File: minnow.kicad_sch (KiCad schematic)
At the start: 66 parts, among them J3 PicoBlade, J3 USB_C_Receptacle_Dev, J3 USB_C_Receptacle_Host, J4 ARM_JTAG_SWD_10_Male, J4 VCCIO_EXT, SW1 SW_DIP_x04, U1 FT230XQ, U2 PI5A3157CEX, U3 PI5A3157CEX, U4 USB3740B-AI2, U5 SiP32432DR3

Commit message: README started
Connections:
- net SWDCLK renamed SWCLK
- net SWDO renamed SWO
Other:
- note added: "Default: SWO and NRESET for full SWD interface. Switched: UART RXD/TXD for USB UART. Can use JP1/2 to isolate from FT or switch RX/TX."
- note removed: "Default: SWDO and NRESET for full SWD interface. Switched: UART RXD/TXD for USB UART. Can use JP1/2 to isolate from FT or switch RX/TX."
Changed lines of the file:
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@@
   (title_block
     (title "Minnow - USB-C DAM Tool")
-    (rev "0")
+    (date "2023-05-19")
+    (rev "1")
     (company "JBR Engineering Research Ltd")
     (comment 1 "J.Whittington 2023")
@@
     (effects (font (size 1.27 1.27) italic) (justify left bottom))
   )
-  (text "Default: SWDO and NRESET for full SWD interface.\nSwitched: UART RXD/TXD for USB UART.\nCan use JP1/2 to isolate from FT or switch RX/TX."
+  (text "Default: SWO and NRESET for full SWD interface.\nSwitched: UART RXD/TXD for USB UART.\nCan use JP1/2 to isolate from FT or switch RX/TX."
     (at 201.168 154.432 0)
     (effects (font (size 1.27 1.27)) (justify left bottom))
@@
     (effects (font (size 1.27 1.27)) (justify right bottom))
   )
-  (label "SWDCLK" (at 350.012 71.374 180) (fields_autoplaced)
+  (label "SWCLK" (at 350.012 71.374 180) (fields_autoplaced)
     (effects (font (size 1.27 1.27)) (justify right bottom))
   )
@@
     (effects (font (size 1.27 1.27)) (justify right bottom))
   )
-  (label "SWDCLK" (at 370.078 202.438 180) (fields_autoplaced)
+  (label "SWCLK" (at 370.078 202.438 180) (fields_autoplaced)
     (effects (font (size 1.27 1.27)) (justify right bottom))
   )
@@
     (effects (font (size 1.27 1.27)) (justify left bottom))
   )
-  (label "SWDO" (at 189.738 220.472 180) (fields_autoplaced)
+  (label "SWO" (at 189.738 220.472 180) (fields_autoplaced)
     (effects (font (size 1.27 1.27)) (justify right bottom))
   )
@@
     (effects (font (size 1.27 1.27)) (justify left bottom))
   )
-  (label "SWDCLK" (at 365.252 158.75 180) (fields_autoplaced)
+  (label "SWCLK" (at 365.252 158.75 180) (fields_autoplaced)
     (effects (font (size 1.27 1.27)) (justify right bottom))
   )
@@
     (effects (font (size 1.27 1.27)) (justify left bottom))
   )
-  (label "SWDO" (at 365.252 161.29 180) (fields_autoplaced)
+  (label "SWO" (at 365.252 161.29 180) (fields_autoplaced)
     (effects (font (size 1.27 1.27)) (justify right bottom))
   )
@@
     (effects (font (size 1.27 1.27)) (justify left bottom))
   )
-  (label "SWDCLK" (at 350.012 86.614 180) (fields_autoplaced)
+  (label "SWCLK" (at 350.012 86.614 180) (fields_autoplaced)
     (effects (font (size 1.27 1.27)) (justify right bottom))
   )
@@
     (effects (font (size 1.27 1.27)) (justify left bottom))
   )
-  (label "SWDO" (at 370.078 207.518 180) (fields_autoplaced)
+  (label "SWO" (at 370.078 207.518 180) (fields_autoplaced)
     (effects (font (size 1.27 1.27)) (justify right bottom))
   )

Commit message: update README for R1 delivery
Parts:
- FB1: MPN LI0603E151R-10 -> LI0603G121R-10; SKU 240-2366-1-ND -> 240-2367-2-ND
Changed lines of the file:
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@@
       (effects (font (size 1.27 1.27)) hide)
     )
-    (property "Description" "150 Ohms @ 100 MHz 1 Power, Signal Line Ferrite Bead 0603 (1608 Metric) 500mA 250mOhm" (at 114.3 40.64 0)
+    (property "Description" "120 Ohms @ 100 MHz 1 Power, Signal Line Ferrite Bead 0603 (1608 Metric) 1A 200mOhm" (at 114.3 40.64 0)
       (effects (font (size 1.27 1.27)) hide)
     )
@@
       (effects (font (size 1.27 1.27)) hide)
     )
-    (property "MPN" "LI0603E151R-10" (at 114.3 40.64 0)
+    (property "MPN" "LI0603G121R-10" (at 114.3 40.64 0)
       (effects (font (size 1.27 1.27)) hide)
     )
-    (property "SKU" "240-2366-1-ND" (at 114.3 40.64 0)
+    (property "SKU" "240-2367-2-ND" (at 114.3 40.64 0)
       (effects (font (size 1.27 1.27)) hide)
     )
@@
       (effects (font (size 1.27 1.27)) hide)
     )
+    (property "Notes" "" (at 114.3 40.64 0)
+      (effects (font (size 1.27 1.27)) hide)
+    )
+    (property "Config" "" (at 114.3 40.64 0)
+      (effects (font (size 1.27 1.27)) hide)
+    )

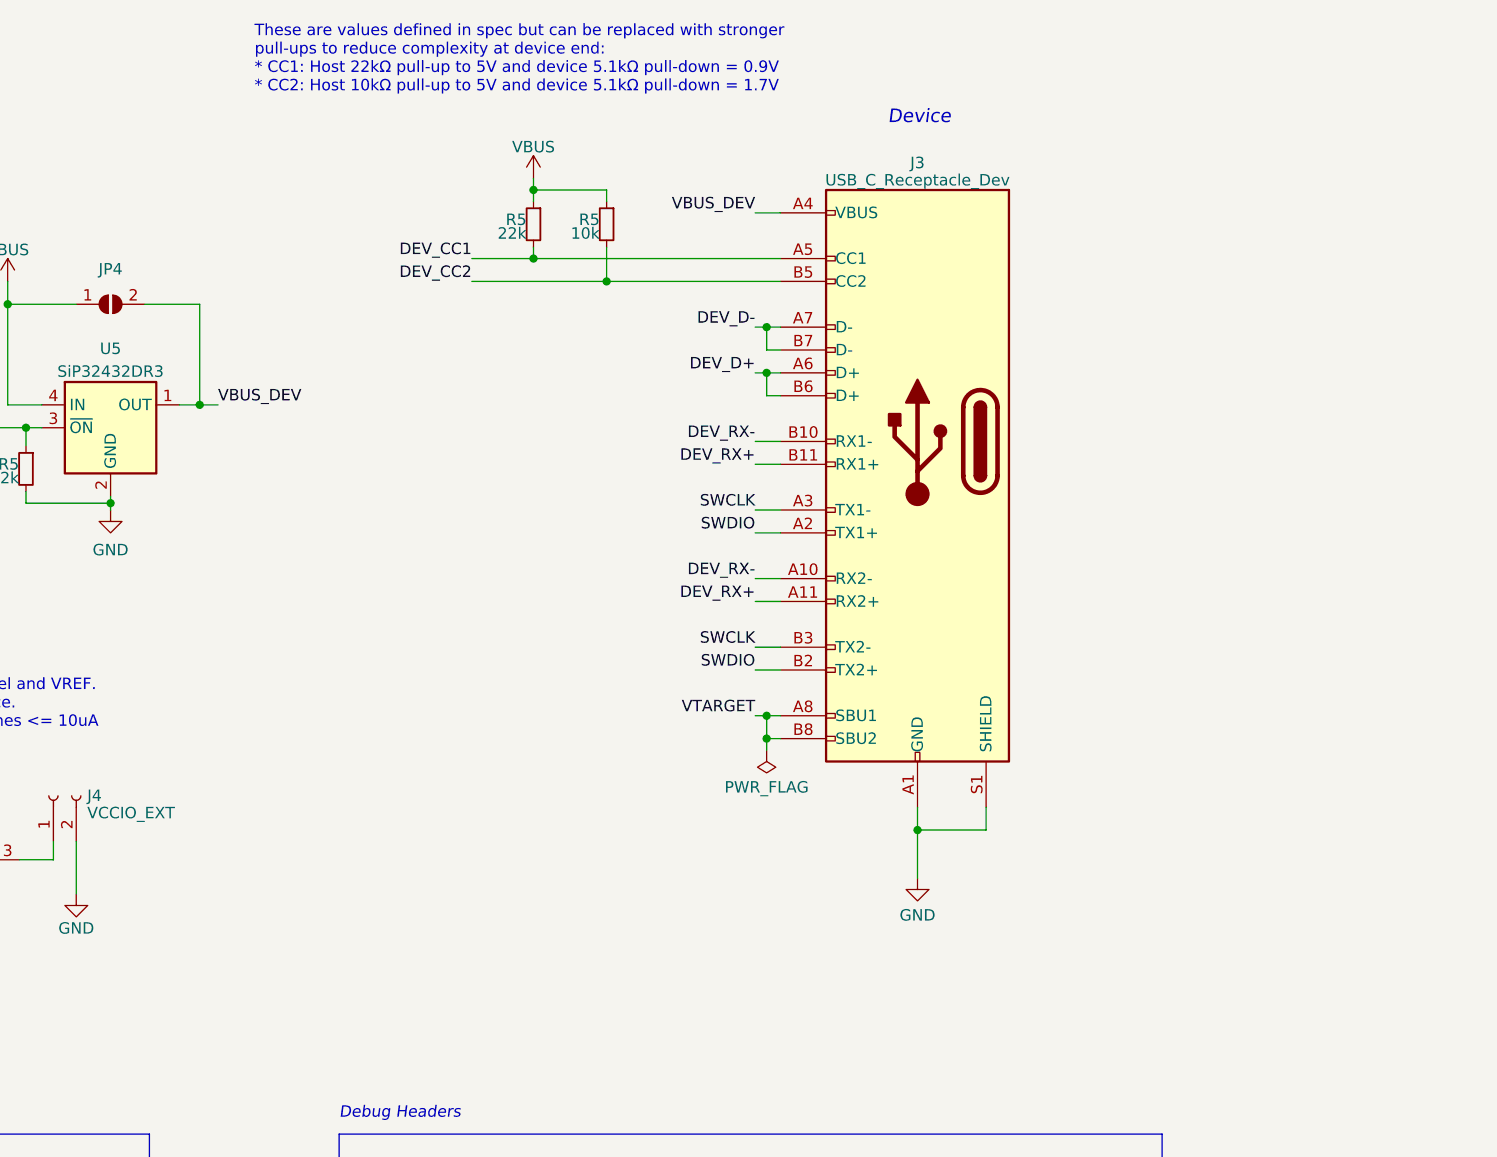
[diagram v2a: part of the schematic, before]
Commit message: plug not receptacle for device (TS)
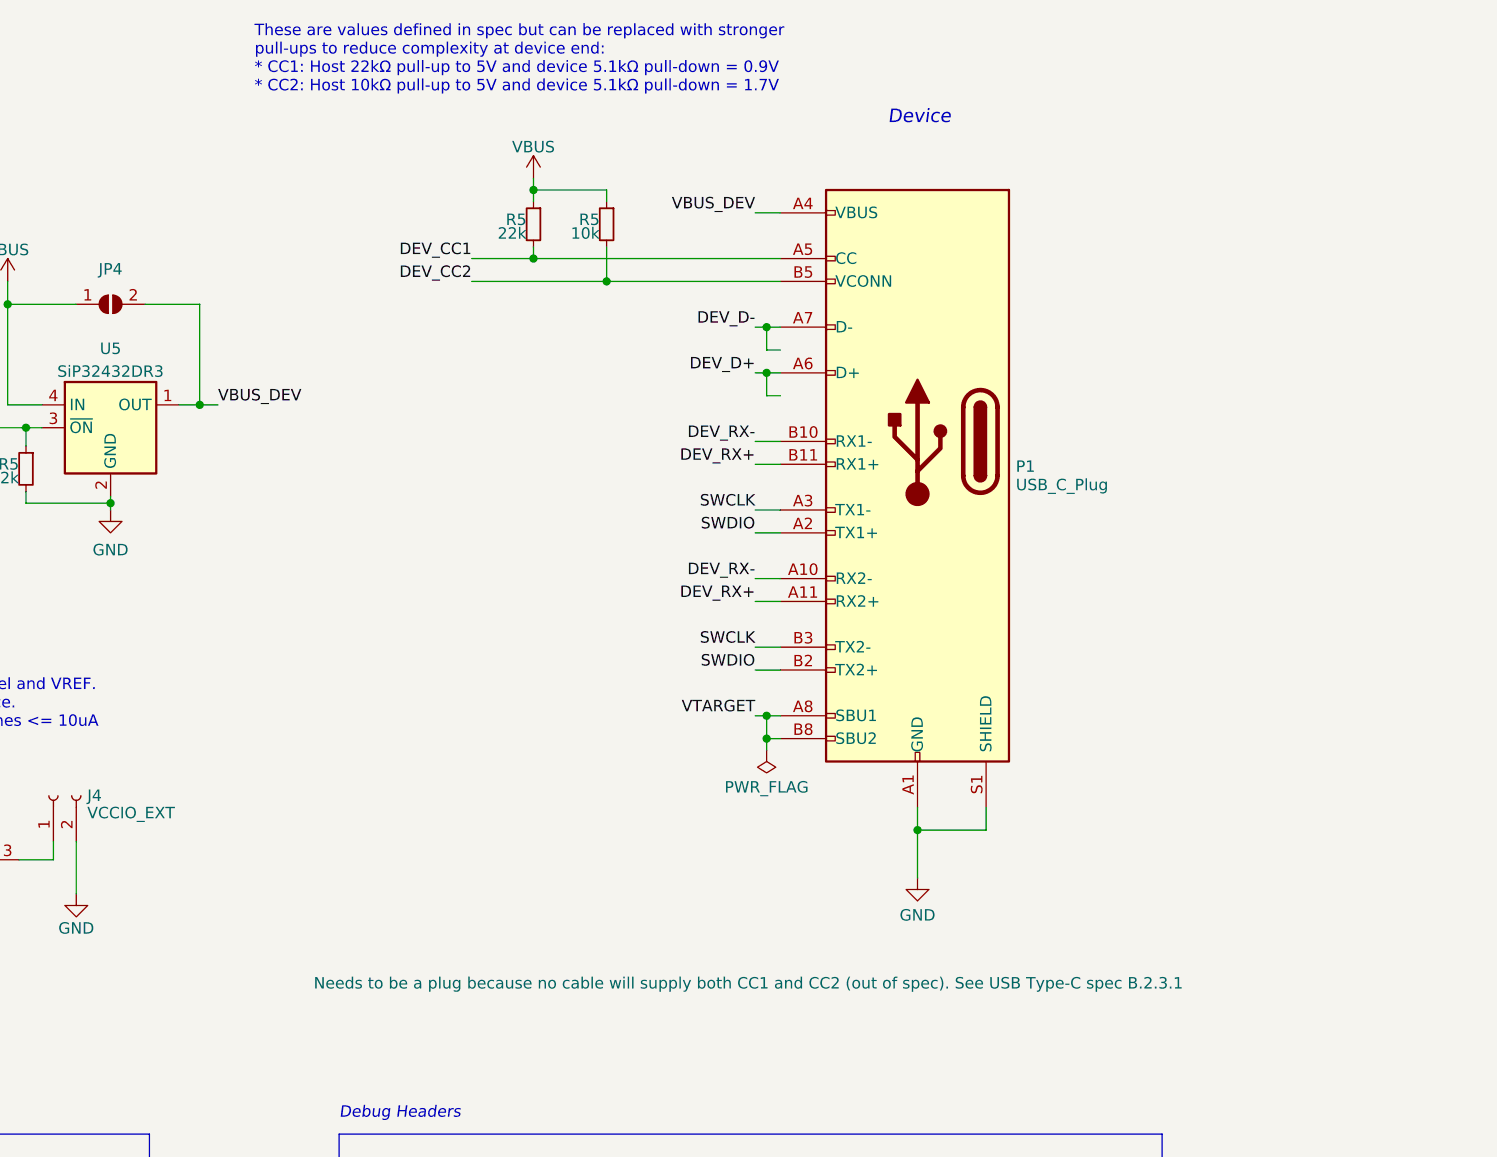
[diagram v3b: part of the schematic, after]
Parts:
- removed J3: USB_C_Receptacle_Dev, Connector_USB:USB_C_Receptacle_Amphenol_12401610E4-2A, symbol Connector:USB_C_Receptacle
- added P1: USB_C_Plug, Connector_USB:USB_C_Plug_Molex_105444, symbol Connector:USB_C_Plug
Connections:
- net DEV_CC1: now also P1.A5 (CC)
- net DEV_CC2: now also P1.B5 (VCONN)
- net DEV_D+: now also P1.A6 (D+)
- net DEV_D-: now also P1.A7 (D-)
- net DEV_RX+: now also P1.A11 (RX2+), P1.B11 (RX1+)
- net DEV_RX-: now also P1.A10 (RX2-), P1.B10 (RX1-)
- net GND: now also P1.A1 (GND), P1.A12 (GND), P1.B1 (GND), P1.B12 (GND), P1.S1 (SHIELD)
- net SWCLK: now also P1.A3 (TX1-), P1.B3 (TX2-)
- net SWDIO: now also P1.A2 (TX1+), P1.B2 (TX2+)
- net VBUS_DEV: now also P1.A4 (VBUS), P1.A9 (VBUS), P1.B4 (VBUS), P1.B9 (VBUS)
- net VTARGET: now also P1.A8 (SBU1), P1.B8 (SBU2)
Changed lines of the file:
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@@
   (title_block
     (title "Minnow - USB-C DAM Tool")
-    (date "2023-05-19")
-    (rev "1")
+    (date "2023-06-22")
+    (rev "2")
     (company "JBR Engineering Research Ltd")
     (comment 1 "J.Whittington 2023")
@@
     )
   )
-  (symbol (lib_id "Connector:USB_C_Receptacle") (at 368.046 63.754 0) (mirror y) (unit 1)
-    (in_bom yes) (on_board yes) (dnp no)
-    (property "Reference" "J3" (at 368.046 32.8041 0)
-      (effects (font (size 1.27 1.27)))
-    )
-    (property "Value" "USB_C_Receptacle_Dev" (at 368.046 34.7251 0)
-      (effects (font (size 1.27 1.27)))
-    )
-    (property "Footprint" "Connector_USB:USB_C_Receptacle_Amphenol_12401610E4-2A" (at 364.236 63.754 0)
-      (effects (font (size 1.27 1.27)) hide)
-    )
-    (property "Datasheet" "https://media.digikey.com/pdf/Data%20Sheets/Amphenol%20PDFs/12401832E402A_Dwg_RevX1_04-25-17.pdf" (at 364.236 63.754 0)
-      (effects (font (size 1.27 1.27)) hide)
-    )
-    (property "Description" "USB-C (USB TYPE-C) USB 3.2 Gen 2 (USB 3.1 Gen 2, Superspeed + (USB 3.1)) Receptacle Connector 24 Position Surface Mount, Right Angle; Through Hole" (at 368.046 63.754 0)
-      (effects (font (size 1.27 1.27)) hide)
-    )
-    (property "MFN" "Amphenol ICC (Commercial Products)" (at 368.046 63.754 0)
-      (effects (font (size 1.27 1.27)) hide)
-    )
-    (property "MPN" "12401610E4#2A" (at 368.046 63.754 0)
-      (effects (font (size 1.27 1.27)) hide)
-    )
-    (property "SKU" "12401610E4#2ACT-ND" (at 368.046 63.754 0)
-      (effects (font (size 1.27 1.27)) hide)
-    )
-    (property "Vendor" "Digkey" (at 368.046 63.754 0)
-      (effects (font (size 1.27 1.27)) hide)
-    )
-    (property "Notes" "" (at 368.046 63.754 0)
-      (effects (font (size 1.27 1.27)) hide)
-    )
-    (property "Config" "" (at 368.046 63.754 0)
-      (effects (font (size 1.27 1.27)) hide)
-    )
-    (property "Characteristics" "" (at 368.046 63.754 0)
-      (effects (font (size 1.27 1.27)) hide)
-    )
-    (pin "A1")
-    (pin "A10")
-    (pin "A11")
-    (pin "A12")
-    (pin "A2")
-    (pin "A3")
-    (pin "A4")
-    (pin "A5")
-    (pin "A6")
-    (pin "A7")
-    (pin "A8")
-    (pin "A9")
-    (pin "B1")
-    (pin "B10")
-    (pin "B11")
-    (pin "B12")
-    (pin "B2")
-    (pin "B3")
-    (pin "B4")
-    (pin "B5")
-    (pin "B6")
-    (pin "B7")
-    (pin "B8")
-    (pin "B9")
-    (pin "S1")
-    (instances
-      (project "USB"
-        (path "/abe08c89-73f7-4625-b1e5-d5b33729a7ca"
-          (reference "J3") (unit 1)
-        )
-      )
-      (project "minnow"
-        (path "/bbabdafc-86d4-4010-b464-a3e83875bd6e"
-          (reference "J2") (unit 1)
-        )
-      )
-      (project "spirit_logger_hardware"
-        (path "/e63e39d7-6ac0-4ffd-8aa3-1841a4541b55/cec0ac2b-8788-4205-bc11-fcadefc26e0e"
-          (reference "J3") (unit 1)
-        )
-      )
-    )
-  )
   (symbol (lib_id "Interface_USB:FT230XQ") (at 73.914 197.104 0) (unit 1)
     (in_bom yes) (on_board yes) (dnp no) (fields_autoplaced)
@@
         )
       )
+    )
+  )
+  (symbol (lib_id "Connector:USB_C_Plug") (at 368.046 63.754 0) (mirror y) (unit 1)
+    (in_bom yes) (on_board yes) (dnp no)
+    (property "Reference" "P1" (at 378.968 66.54 0)
+      (effects (font (size 1.27 1.27)) (justify right))
+    )
+    (property "Value" "USB_C_Plug" (at 378.968 68.588 0)
+      (effects (font (size 1.27 1.27)) (justify right))
+    )
+    (property "Footprint" "Connector_USB:USB_C_Plug_Molex_105444" (at 364.236 63.754 0)
+      (effects (font (size 1.27 1.27)) hide)
+    )
+    (property "Datasheet" "https://www.molex.com/content/dam/molex/molex-dot-com/products/automated/en-us/salesdrawingpdf/105/105444/1054440001_sd.pdf?inline" (at 364.236 63.754 0)
+      (effects (font (size 1.27 1.27)) hide)
+    )
+    (property "MFN" "Molex" (at 368.046 63.754 0)
+      (effects (font (size 1.27 1.27)) hide)
+    )
+    (property "MPN" "1054440011" (at 368.046 63.754 0)
+      (effects (font (size 1.27 1.27)) hide)
+    )
+    (property "Description" "USB-C (USB TYPE-C) USB 3.2 Gen 2 (USB 3.1 Gen 2, Superspeed + (USB 3.1)) Plug Connector 24 Position Board Edge, Straddle Mount" (at 368.046 63.754 0)
+      (effects (font (size 1.27 1.27)) hide)
+    )
+    (property "Notes" "Needs to be a plug because no cable will supply both CC1 and CC2 (out of spec). See USB Type-C spec B.2.3.1" (at 349.25 123.952 0)
+      (effects (font (size 1.27 1.27)))
+    )
+    (property "Config" "" (at 368.046 63.754 0)
+      (effects (font (size 1.27 1.27)) hide)
+    )
+    (property "Vendor" "Digikey" (at 368.046 63.754 0)
+      (effects (font (size 1.27 1.27)) hide)
+    )
+    (property "SKU" "900-1054440011CT-ND" (at 368.046 63.754 0)
+      (effects (font (size 1.27 1.27)) hide)
+    )
+    (property "Characteristics" "" (at 368.046 63.754 0)
+      (effects (font (size 1.27 1.27)) hide)
+    )
+    (pin "A1")
+    (pin "A10")
+    (pin "A11")
+    (pin "A12")
+    (pin "A2")
+    (pin "A3")
+    (pin "A4")
+    (pin "A5")
+    (pin "A6")
+    (pin "A7")
+    (pin "A8")
+    (pin "A9")
+    (pin "B1")
+    (pin "B10")
+    (pin "B11")
+    (pin "B12")
+    (pin "B2")
+    (pin "B3")
+    (pin "B4")
+    (pin "B5")
+    (pin "B8")
+    (pin "B9")
+    (pin "S1")
+    (instances
+      (project "minnow"
+        (path "/bbabdafc-86d4-4010-b464-a3e83875bd6e"
+          (reference "P1") (unit 1)
+        )
+      )

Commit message: pcb render
active layers
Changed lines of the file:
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@@
   (junction (at 42.672 186.944) (diameter 0) (color 0 0 0 0)
   )
-  (junction (at 351.282 56.134) (diameter 0) (color 0 0 0 0)
-  )
   (junction (at 107.95 40.64) (diameter 0) (color 0 0 0 0)
   )
@@
   )
   (junction (at 349.758 222.504) (diameter 0) (color 0 0 0 0)
-  )
-  (junction (at 351.282 51.054) (diameter 0) (color 0 0 0 0)
   )
   (junction (at 109.728 207.264) (diameter 0) (color 0 0 0 0)
@@
   (no_connect (at 64.516 66.04))
   (no_connect (at 64.516 88.9))
-  (wire (pts (xy 352.806 58.674) (xy 351.282 58.674))
-    (stroke (width 0) (type default))
-  )
   (wire (pts (xy 76.454 217.424) (xy 76.454 219.71))
     (stroke (width 0) (type default))
@@
     (stroke (width 0) (type default))
   )
-  (wire (pts (xy 351.282 58.674) (xy 351.282 56.134))
-    (stroke (width 0) (type default))
-  )
   (wire (pts (xy 144.526 97.282) (xy 144.526 107.442))
     (stroke (width 0) (type default))
@@
     (stroke (width 0) (type default))
   )
-  (wire (pts (xy 352.806 53.594) (xy 351.282 53.594))
-    (stroke (width 0) (type default))
-  )
   (wire (pts (xy 178.308 74.676) (xy 185.928 74.676))
     (stroke (width 0) (type default))
@@
     (stroke (width 0) (type default))
   )
-  (wire (pts (xy 351.282 51.054) (xy 352.806 51.054))
+  (wire (pts (xy 350.012 51.054) (xy 352.806 51.054))
     (stroke (width 0) (type default))
   )
@@
     (stroke (width 0) (type default))
   )
-  (wire (pts (xy 350.012 51.054) (xy 351.282 51.054))
-    (stroke (width 0) (type default))
-  )
   (wire (pts (xy 189.738 220.472) (xy 203.2 220.472))
     (stroke (width 0) (type default))
@@
     (stroke (width 0) (type default))
   )
-  (wire (pts (xy 351.282 56.134) (xy 352.806 56.134))
-    (stroke (width 0) (type default))
-  )
   (wire (pts (xy 73.914 217.424) (xy 76.454 217.424))
     (stroke (width 0) (type default))
@@
     (stroke (width 0) (type default))
   )
-  (wire (pts (xy 351.282 53.594) (xy 351.282 51.054))
-    (stroke (width 0) (type default))
-  )
   (wire (pts (xy 144.526 112.522) (xy 155.194 112.522))
     (stroke (width 0) (type default))
@@
     (stroke (width 0) (type default))
   )
-  (wire (pts (xy 350.012 56.134) (xy 351.282 56.134))
-    (stroke (width 0) (type default))
-  )
+  (wire (pts (xy 350.012 56.134) (xy 352.806 56.134))
+    (stroke (width 0) (type default))
+  )
